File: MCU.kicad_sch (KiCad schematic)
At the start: 16 parts, among them U10 MCP23017_ML, U11 ESP32-C6-WROOM-1, U12 KMR241GLFS, U13 KMR241GLFS, U5 CD74HC4067M, Y1 32.768kHz 9pF

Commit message: pcb / inital work
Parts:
- C27, C28: footprint Capacitor_THT:C_Disc_D3.0mm_W2.0mm_P2.50mm -> Capacitor_SMD:C_0402_1005Metric
- C50: footprint Capacitor_THT:C_Disc_D3.0mm_W2.0mm_P2.50mm -> Capacitor_SMD:C_0603_1608Metric
- JP1, JP2, JP5: footprint (none) -> PCM_Jumper_AKL:Jumper_P2.54mm_D0.7mm
- R25, R28, R37, R7: footprint (none) -> Resistor_SMD:R_0603_1608Metric
- U12, U13: footprint SWITCH_241GLFS -> uwu:SWITCH_241GLFS
- Y1: footprint (none) -> uwu:XTAL_ASE-24.576MHZ-LC-T
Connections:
- net SD_SW: now also U5.19 (I12); no longer U10.18 (GPA1)
- net JACK_LINE_SW: now reaches U5.18 (I13)
- net SWITCH_1: now reaches U10.22 (GPA5)
- net SWITCH_2: now reaches U10.23 (GPA6)
- net SWITCH_3: now reaches U10.24 (GPA7)
- new net AUDIO_EN: U10.18 (GPA1)
- no-connect marks 7 -> 4

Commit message: ICs placed
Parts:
- Y1: footprint uwu:XTAL_ASE-24.576MHZ-LC-T -> Crystal:Crystal_SMD_0603-2Pin_6.0x3.5mm
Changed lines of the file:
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@@
+			)
+		)
+		(property "OPTION" ""
+			(at 144.78 134.62 0)
+			(effects
+				(font
+					(size 1.27 1.27)
+				)
+				(hide yes)
 			)
 		)
@@
 			)
 		)
+		(property "OPTION" ""
+			(at 142.24 74.93 0)
+			(effects
+				(font
+					(size 1.27 1.27)
+				)
+				(hide yes)
+			)
+		)
 		(pin "2"
 		)
@@
 			)
 		)
+		(property "OPTION" ""
+			(at 124.46 80.01 0)
+			(effects
+				(font
+					(size 1.27 1.27)
+				)
+				(hide yes)
+			)
+		)
 		(pin "1"
 		)
@@
 			)
 		)
+		(property "OPTION" ""
+			(at 137.16 114.3 0)
+			(effects
+				(font
+					(size 1.27 1.27)
+				)
+				(hide yes)
+			)
+		)
 		(pin "4"
 		)
@@
 			)
 		)
+		(property "OPTION" ""
+			(at 149.86 80.01 0)
+			(effects
+				(font
+					(size 1.27 1.27)
+				)
+				(hide yes)
+			)
+		)
 		(pin "2"
 		)
@@
 			)
 		)
+		(property "OPTION" ""
+			(at 49.53 152.4 0)
+			(effects
+				(font
+					(size 1.27 1.27)
+				)
+				(hide yes)
+			)
+		)
 		(pin "8"
 		)
@@
 			)
 		)
+		(property "OPTION" ""
+			(at 149.86 69.85 0)
+			(effects
+				(font
+					(size 1.27 1.27)
+				)
+				(hide yes)
+			)
+		)
 		(pin "2"
 		)
@@
 			)
 		)
+		(property "OPTION" ""
+			(at 69.85 85.09 0)
+			(effects
+				(font
+					(size 1.27 1.27)
+				)
+				(hide yes)
+			)
+		)
 		(pin "16"
 		)
@@
 			)
 		)
+		(property "OPTION" ""
+			(at 198.12 62.23 0)
+			(effects
+				(font
+					(size 1.27 1.27)
+				)
+				(hide yes)
+			)
+		)
 		(pin "1"
 		)
@@
 			)
 		)
-		(property "Footprint" "uwu:XTAL_ASE-24.576MHZ-LC-T"
+		(property "Footprint" "Crystal:Crystal_SMD_0603-2Pin_6.0x3.5mm"
 			(at 130.81 74.93 0)
 			(effects
@@
 		)
 		(property "Specifications" ""
+			(at 130.81 74.93 0)
+			(effects
+				(font
+					(size 1.27 1.27)
+				)
+				(hide yes)
+			)
+		)
+		(property "OPTION" ""
 			(at 130.81 74.93 0)
 			(effects
@@
 			)
 		)
+		(property "OPTION" ""
+			(at 124.46 69.85 0)
+			(effects
+				(font
+					(size 1.27 1.27)
+				)
+				(hide yes)
+			)
+		)
 		(pin "1"
 		)
@@
 			)
 		)
+		(property "OPTION" ""
+			(at 226.06 100.33 0)
+			(effects
+				(font
+					(size 1.27 1.27)
+				)
+				(hide yes)
+			)
+		)
 		(pin "26"
 		)
@@
 			)
 		)
+		(property "OPTION" ""
+			(at 165.1 64.77 0)
+			(effects
+				(font
+					(size 1.27 1.27)
+				)
+				(hide yes)
+			)
+		)
 		(pin "1"
 		)
@@
 			)
 		)
+		(property "OPTION" ""
+			(at 189.23 69.85 0)
+			(effects
+				(font
+					(size 1.27 1.27)
+				)
+				(hide yes)
+			)
+		)
 		(pin "2"
 		)
@@
 			)
 		)
+		(property "OPTION" ""
+			(at 182.88 67.31 0)
+			(effects
+				(font
+					(size 1.27 1.27)
+				)
+				(hide yes)
+			)
+		)
 		(pin "1"
 		)
@@
 			(at 173.99 64.77 0)
 			(effects
+				(font
+					(size 1.27 1.27)
+				)
+				(hide yes)
+			)
+		)
+		(property "OPTION" ""
+			(at 173.99 64.77 0)
+			(effects

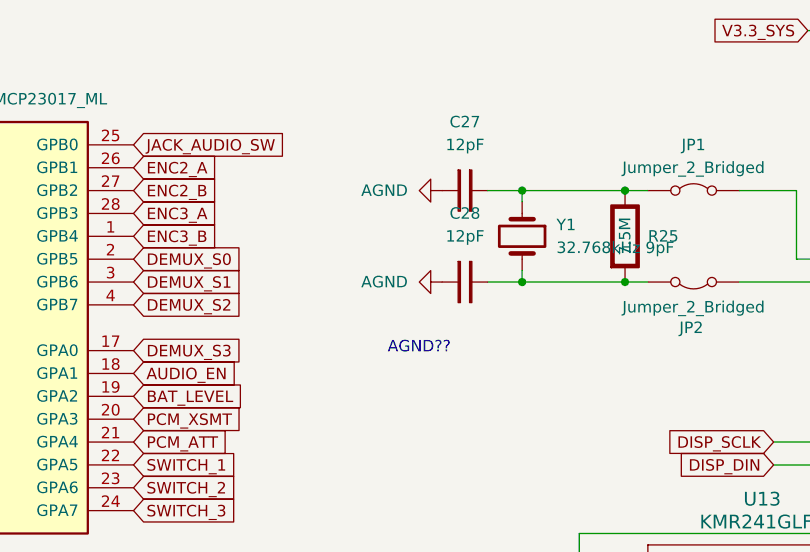
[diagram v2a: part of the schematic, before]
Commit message: all pcb elements positioned + minor schematics changes
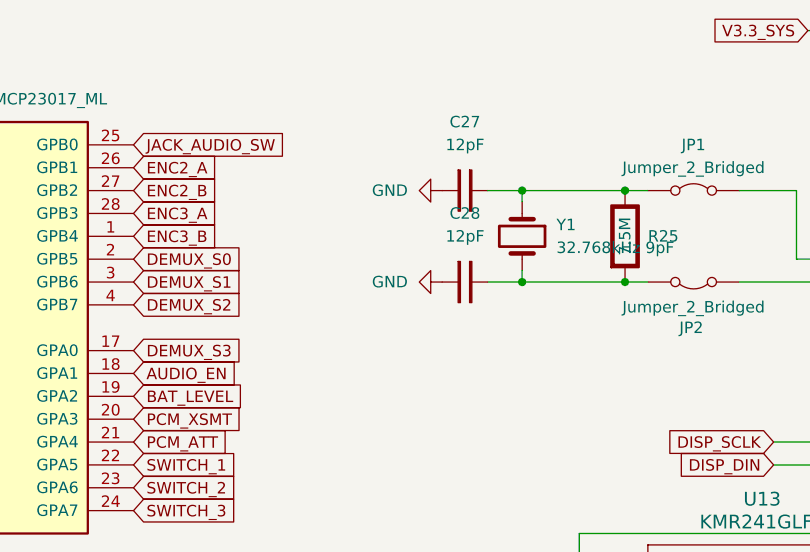
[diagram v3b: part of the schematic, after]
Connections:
- net AGND is gone; now on net GND: C27.1, C28.1
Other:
- note removed: "AGND??"
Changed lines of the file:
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@@
-		)
-	)
-	(text "AGND??"
-		(exclude_from_sim no)
-		(at 119.38 87.376 0)
-		(effects
-			(font
-				(size 1.27 1.27)
-			)
 		)
 	)
@@
 			)
 		)
-		(property "Value" "AGND"
+		(property "Value" "GND"
 			(at 118.11 69.8499 90)
 			(effects
@@
 			)
 		)
-		(property "Value" "AGND"
+		(property "Value" "GND"
 			(at 118.11 80.0099 90)
 			(effects

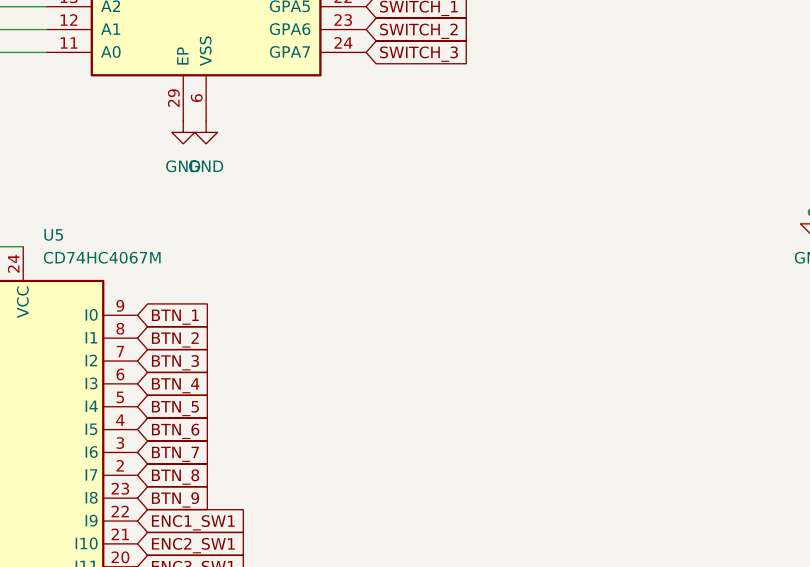
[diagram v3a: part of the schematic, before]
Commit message: changing ic placement
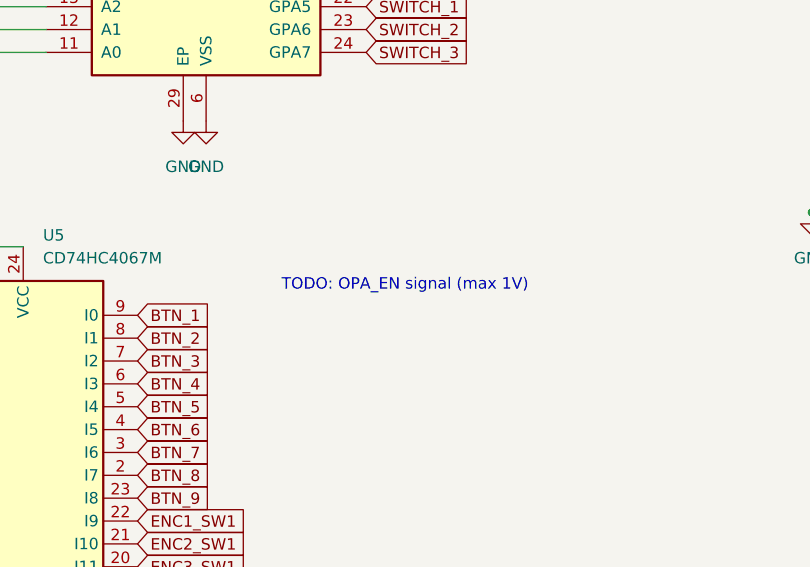
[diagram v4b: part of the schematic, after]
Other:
- note added: "TODO: OPA_EN signal (max 1V)"
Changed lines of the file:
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@@
+		)
+	)
+	(text "TODO: OPA_EN signal (max 1V)"
+		(exclude_from_sim no)
+		(at 91.948 131.318 0)
+		(effects
+			(font
+				(size 1.27 1.27)
+			)
 		)
 	)

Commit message: routing
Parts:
- removed JP1, JP2, JP5: Jumper_2_Bridged, PCM_Jumper_AKL:Jumper_P2.54mm_D0.7mm, symbol Jumper:Jumper_2_Bridged
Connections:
- net BAT_LEVEL: now also U5.17 (I14); no longer U10.19 (GPA2)
- net V3.3_SYS: now also C50.1, R37.2 (-), U11.3 (EN/CHIP_PU), U12.1, U12.4
- net at C27.2, R25.1 (+), Y1.1: now also U11.8 (GPIO0/ADC1_CH0/XTAL_32K_P), U13.1, U13.4
- net at C28.2, R25.2 (-), Y1.2: now also U11.9 (GPIO1/ADC1_CH1/XTAL_32K_N)
- net AUDIO_EN renamed JACK_EN
- new net LINEOUT_EN: U10.19 (GPA2)
- no-connect marks 4 -> 3
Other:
- note removed: "TODO: OPA_EN signal (max 1V)"
